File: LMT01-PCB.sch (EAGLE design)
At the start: 27 parts, among them IC1 PIC18F47K40, IC2 +12v, IC3 LM393D, IC4 MAX3467CPA, IC5 LM393D

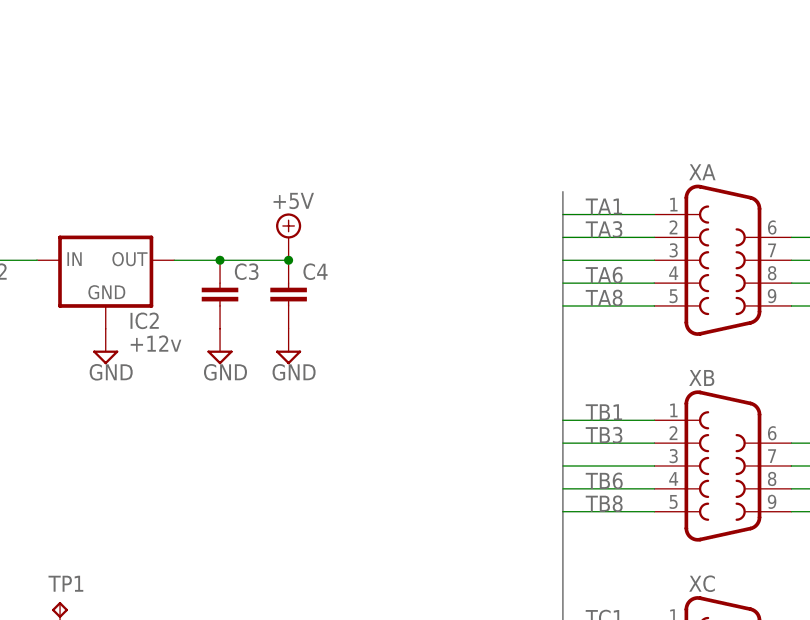
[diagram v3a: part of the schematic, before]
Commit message: Adding power LED
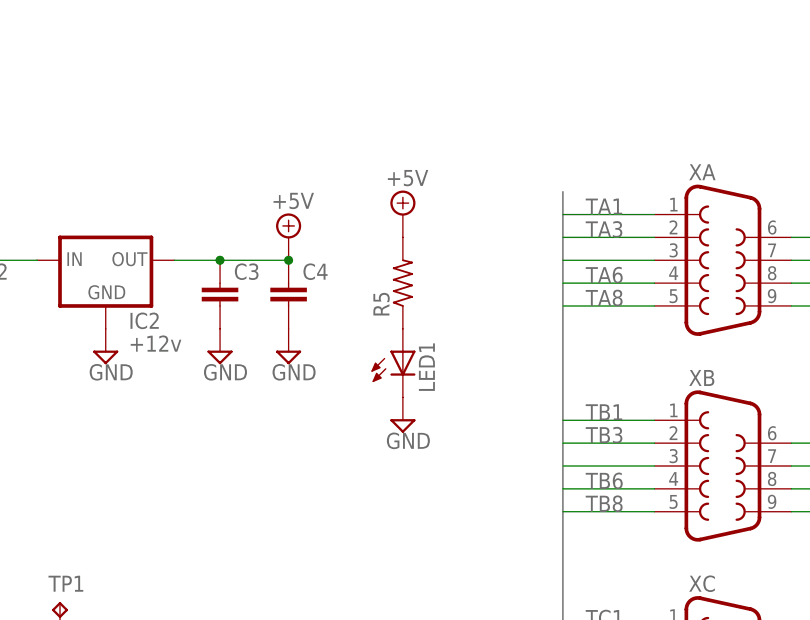
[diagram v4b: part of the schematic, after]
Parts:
- added LED1: (no value), led:LEDCHIPLED_1206
- added R5: (no value), resistor:R-US_R1206
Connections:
- new net N$5: LED1.A, R5.1
- net +5V: now also R5.2
- net GND: now also LED1.C
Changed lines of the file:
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@@
 <part name="JP4" library="SparkFun-Jumpers" deviceset="JUMPER-SMT_2_NO" device="_SILK"/>
 <part name="JP5" library="SparkFun-Jumpers" deviceset="JUMPER-SMT_2_NO" device="_SILK"/>
+<part name="LED1" library="led" deviceset="LED" device="CHIPLED_1206"/>
+<part name="R5" library="resistor" deviceset="R-US_" device="R1206"/>
+<part name="SUPPLY32" library="supply2" deviceset="GND" device=""/>
+<part name="SUPPLY33" library="supply2" deviceset="+5V" device=""/>
 </parts>
 <sheets>
@@
 <instance part="JP4" gate="G$1" x="111.76" y="-35.56"/>
 <instance part="JP5" gate="G$1" x="154.94" y="-35.56"/>
+<instance part="LED1" gate="G$1" x="-7.62" y="10.16"/>
+<instance part="R5" gate="G$1" x="-7.62" y="17.78" rot="R90"/>
+<instance part="SUPPLY32" gate="GND" x="-7.62" y="2.54"/>
+<instance part="SUPPLY33" gate="+5V" x="-7.62" y="25.4"/>
 </instances>
 <busses>
@@
 <pinref part="SUPPLY29" gate="+5V" pin="+5V"/>
 </segment>
+<segment>
+<pinref part="R5" gate="G$1" pin="2"/>
+<pinref part="SUPPLY33" gate="+5V" pin="+5V"/>
+</segment>
 </net>
 <net name="GND" class="0">
@@
 <pinref part="IC5" gate="P" pin="V-"/>
 <pinref part="SUPPLY31" gate="GND" pin="GND"/>
+</segment>
+<segment>
+<pinref part="LED1" gate="G$1" pin="C"/>
+<pinref part="SUPPLY32" gate="GND" pin="GND"/>
 </segment>
 </net>
@@
 </segment>
 </net>
+<net name="N$5" class="0">
+<segment>
+<pinref part="LED1" gate="G$1" pin="A"/>
+<pinref part="R5" gate="G$1" pin="1"/>
+</segment>
+</net>

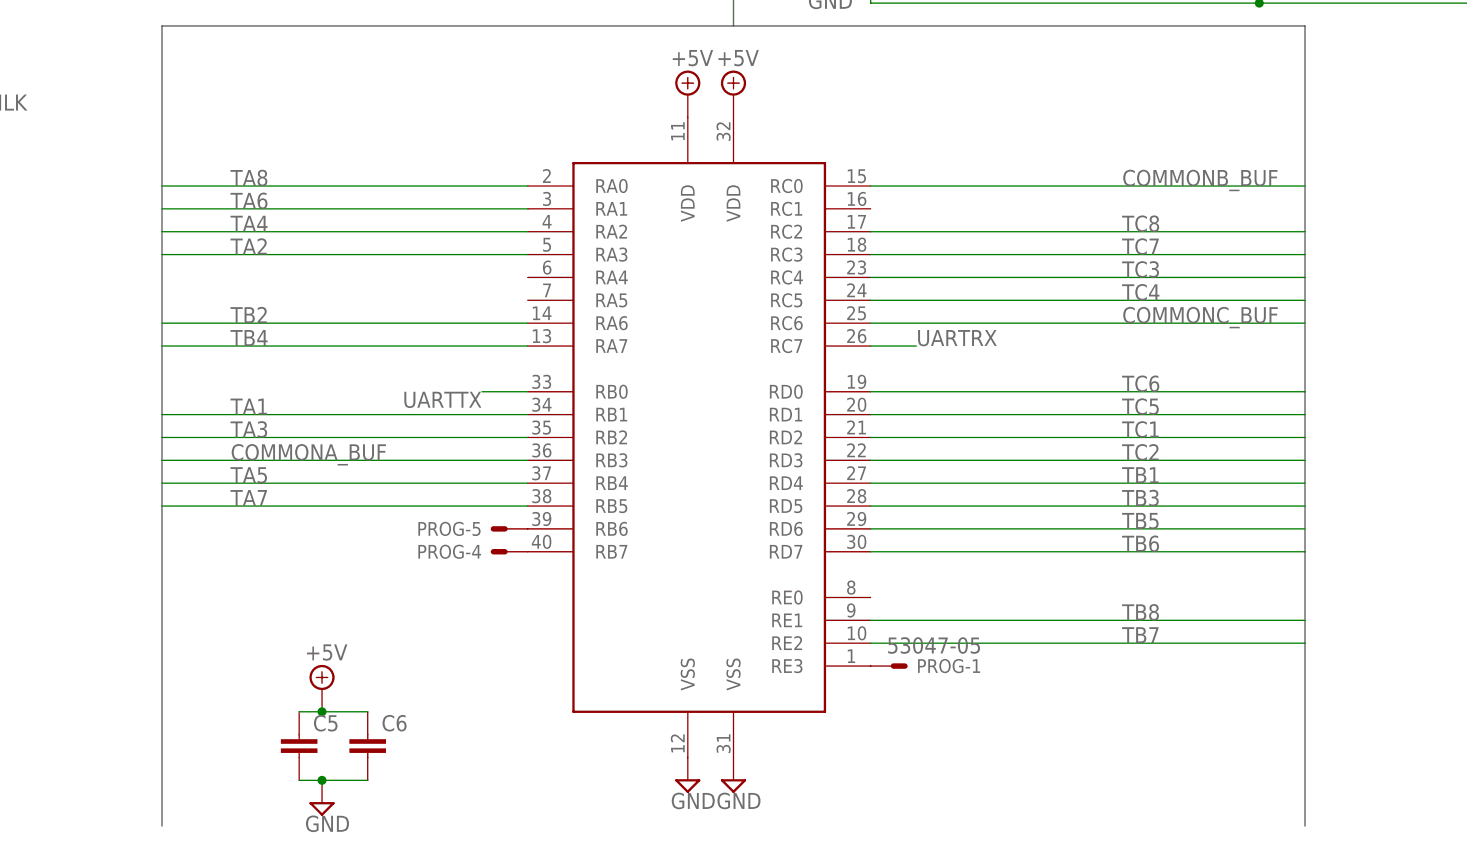
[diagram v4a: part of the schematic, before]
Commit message: Upgrading to PIC18F47Q84
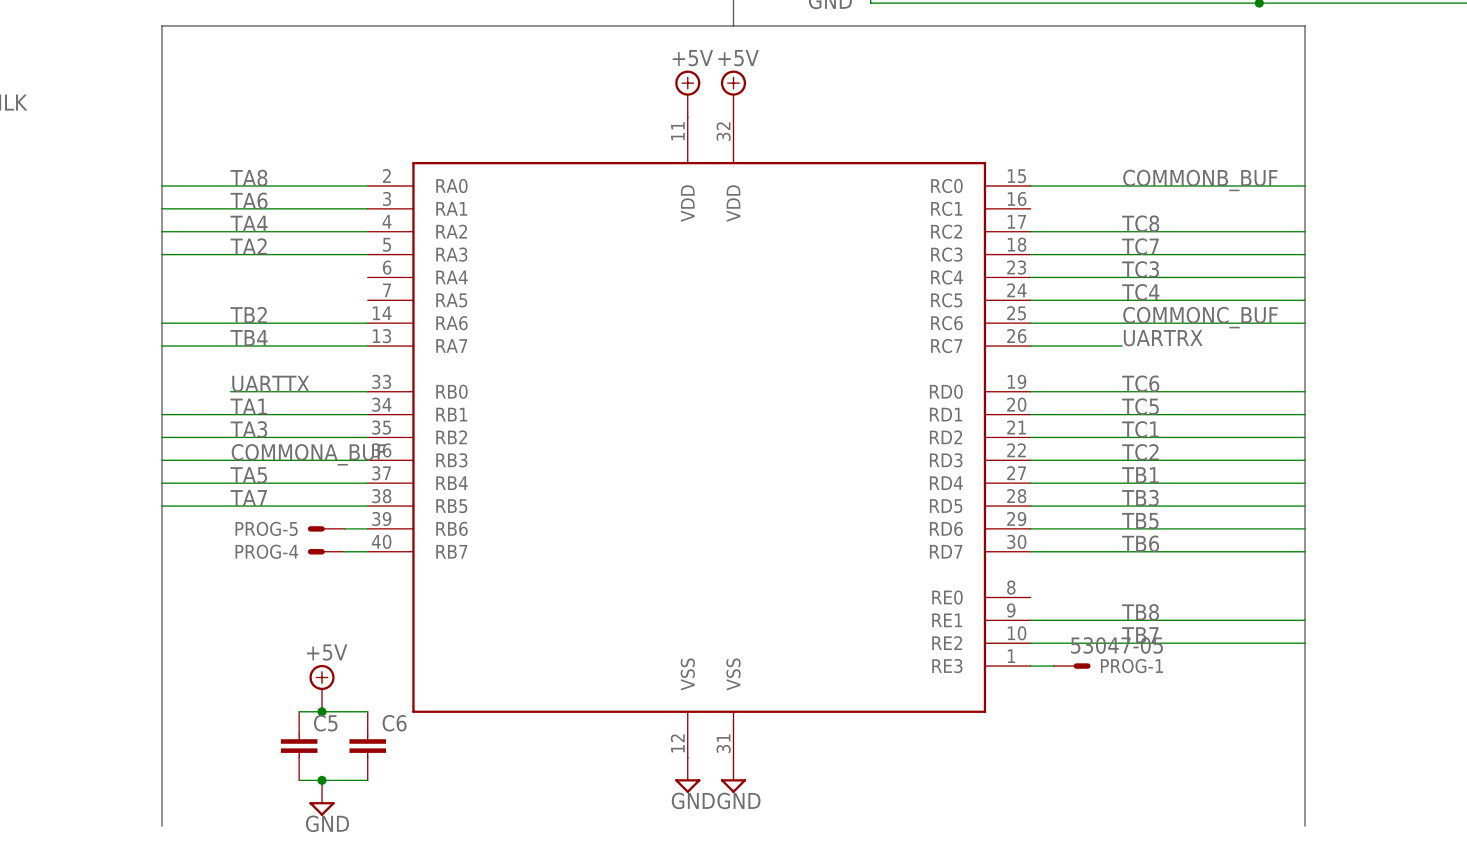
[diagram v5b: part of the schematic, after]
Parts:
- IC1: value PIC18F47K40 -> PIC18F47Q84; device microchip:PIC18F47K40 -> FRC696:PIC18F47Q84
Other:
- moved on the sheet: PROG-1, PROG-4, PROG-5

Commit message: Pin names
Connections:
- net N$1: now also IC1.RE3/!MCLR; no longer IC1.RE3
- net N$2: now also IC1.RB7/PGD; no longer IC1.RB7
- net N$3: now also IC1.RB6/PGC; no longer IC1.RB6
- net TB2: now also IC1.RA6/CLKOUT; no longer IC1.RA6
- net TB4: now also IC1.RA7/CLKIN; no longer IC1.RA7
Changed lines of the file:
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@@
 </segment>
 <segment>
-<pinref part="IC1" gate="G$1" pin="RA6"/>
+<pinref part="IC1" gate="G$1" pin="RA6/CLKOUT"/>
 <wire x1="5.08" y1="-106.68" x2="-17.78" y2="-106.68" width="0.1524" layer="91"/>
 <label x="-10.16" y="-106.68" size="1.778" layer="95"/>
@@
 </segment>
 <segment>
-<pinref part="IC1" gate="G$1" pin="RA7"/>
+<pinref part="IC1" gate="G$1" pin="RA7/CLKIN"/>
 <wire x1="5.08" y1="-109.22" x2="-17.78" y2="-109.22" width="0.1524" layer="91"/>
 <label x="-10.16" y="-109.22" size="1.778" layer="95"/>
@@
 <net name="N$1" class="0">
 <segment>
-<pinref part="IC1" gate="G$1" pin="RE3"/>
+<pinref part="IC1" gate="G$1" pin="RE3/!MCLR"/>
 <pinref part="PROG" gate="-1" pin="S"/>
 <wire x1="81.28" y1="-144.78" x2="78.74" y2="-144.78" width="0.1524" layer="91"/>
@@
 <net name="N$2" class="0">
 <segment>
-<pinref part="IC1" gate="G$1" pin="RB7"/>
+<pinref part="IC1" gate="G$1" pin="RB7/PGD"/>
 <pinref part="PROG" gate="-4" pin="S"/>
 <wire x1="2.54" y1="-132.08" x2="5.08" y2="-132.08" width="0.1524" layer="91"/>
@@
 <net name="N$3" class="0">
 <segment>
-<pinref part="IC1" gate="G$1" pin="RB6"/>
+<pinref part="IC1" gate="G$1" pin="RB6/PGC"/>
 <pinref part="PROG" gate="-5" pin="S"/>
 <wire x1="2.54" y1="-129.54" x2="5.08" y2="-129.54" width="0.1524" layer="91"/>

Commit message: Adding test points
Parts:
- added TP3, TP4, TP5: TPB1,27, testpad:TPB1,27
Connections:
- net N$21 renamed TX+
- net N$22 renamed TX-
- net N$23 renamed RX+
- net N$24 renamed RX-
- new net N$6: IC1.RA5, TP4.TP
- new net N$7: IC1.RE0, TP5.TP
- net N$4: now also TP3.TP
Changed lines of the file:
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@@
 <part name="SUPPLY32" library="supply2" deviceset="GND" device=""/>
 <part name="SUPPLY33" library="supply2" deviceset="+5V" device=""/>
+<part name="TP3" library="testpad" deviceset="TP" device="B1,27"/>
+<part name="TP4" library="testpad" deviceset="TP" device="B1,27"/>
+<part name="TP5" library="testpad" deviceset="TP" device="B1,27"/>
 </parts>
 <sheets>
@@
 <instance part="SUPPLY32" gate="GND" x="-7.62" y="2.54"/>
 <instance part="SUPPLY33" gate="+5V" x="-7.62" y="25.4"/>
+<instance part="TP3" gate="G$1" x="170.18" y="-68.58"/>
+<instance part="TP4" gate="G$1" x="2.54" y="-104.14" rot="R90"/>
+<instance part="TP5" gate="G$1" x="81.28" y="-137.16" rot="R270"/>
 </instances>
 <busses>
@@
 </segment>
 </net>
-<net name="N$21" class="0">
+<net name="TX+" class="0">
 <segment>
 <pinref part="IC4" gate="G$1" pin="Y"/>
@@
 </segment>
 </net>
-<net name="N$22" class="0">
+<net name="TX-" class="0">
 <segment>
 <pinref part="IC4" gate="G$1" pin="Z"/>
@@
 </segment>
 </net>
-<net name="N$23" class="0">
+<net name="RX+" class="0">
 <segment>
 <pinref part="IC4" gate="G$1" pin="A"/>
@@
 </segment>
 </net>
-<net name="N$24" class="0">
+<net name="RX-" class="0">
 <segment>
 <pinref part="IC4" gate="G$1" pin="B"/>
@@
 <pinref part="XA" gate="G$1" pin="3"/>
 <wire x1="20.32" y1="20.32" x2="10.16" y2="20.32" width="0.1524" layer="91"/>
+<label x="12.7" y="20.32" size="1.778" layer="95"/>
 </segment>
 <segment>
@@
 <pinref part="IC5" gate="A" pin="-IN"/>
 <wire x1="104.14" y1="-71.12" x2="144.78" y2="-71.12" width="0.1524" layer="91"/>
-<wire x1="144.78" y1="-71.12" x2="185.42" y2="-71.12" width="0.1524" layer="91"/>
+<wire x1="144.78" y1="-71.12" x2="170.18" y2="-71.12" width="0.1524" layer="91"/>
+<wire x1="170.18" y1="-71.12" x2="185.42" y2="-71.12" width="0.1524" layer="91"/>
 <wire x1="104.14" y1="-53.34" x2="104.14" y2="-71.12" width="0.1524" layer="91"/>
 <junction x="104.14" y="-71.12"/>
@@
 <wire x1="144.78" y1="-53.34" x2="144.78" y2="-71.12" width="0.1524" layer="91"/>
 <junction x="144.78" y="-71.12"/>
+<pinref part="TP3" gate="G$1" pin="TP"/>
+<junction x="170.18" y="-71.12"/>
 </segment>
 </net>
@@
 </segment>
 </net>
+<net name="N$6" class="0">
+<segment>
+<pinref part="IC1" gate="G$1" pin="RA5"/>
+<pinref part="TP4" gate="G$1" pin="TP"/>
+</segment>
+</net>
+<net name="N$7" class="0">
+<segment>
+<pinref part="IC1" gate="G$1" pin="RE0"/>
+<pinref part="TP5" gate="G$1" pin="TP"/>
+</segment>
+</net>

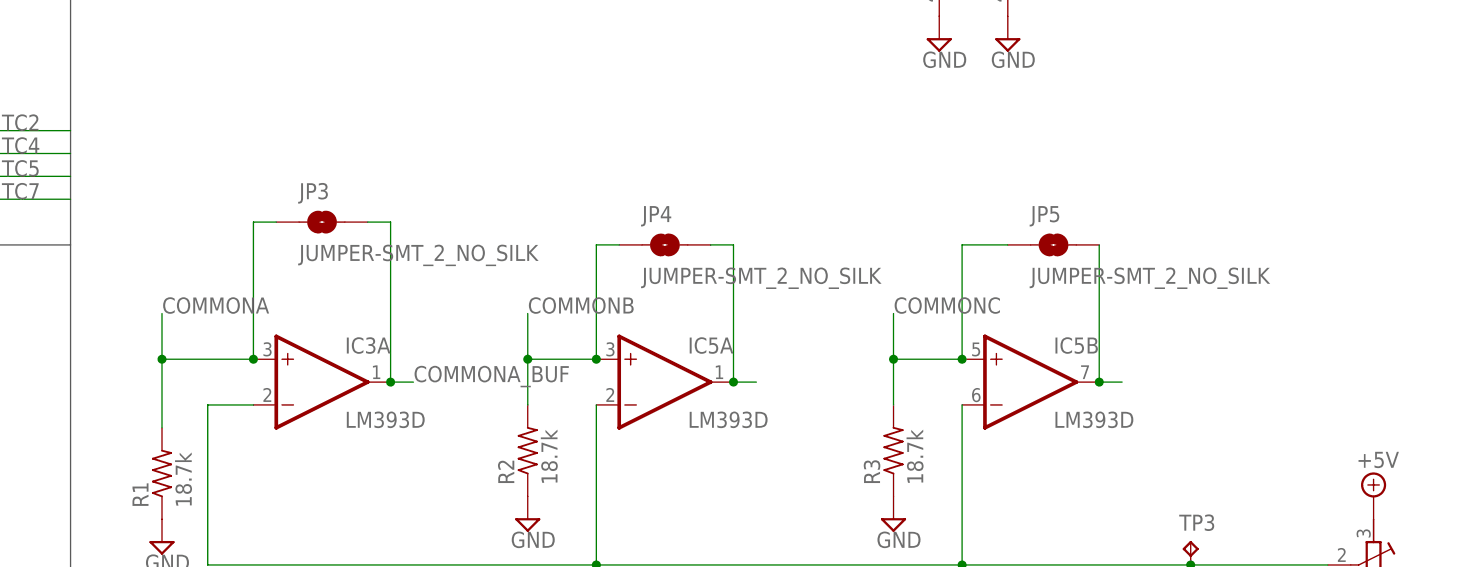
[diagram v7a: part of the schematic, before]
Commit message: Adding more test points and deleting jumpers
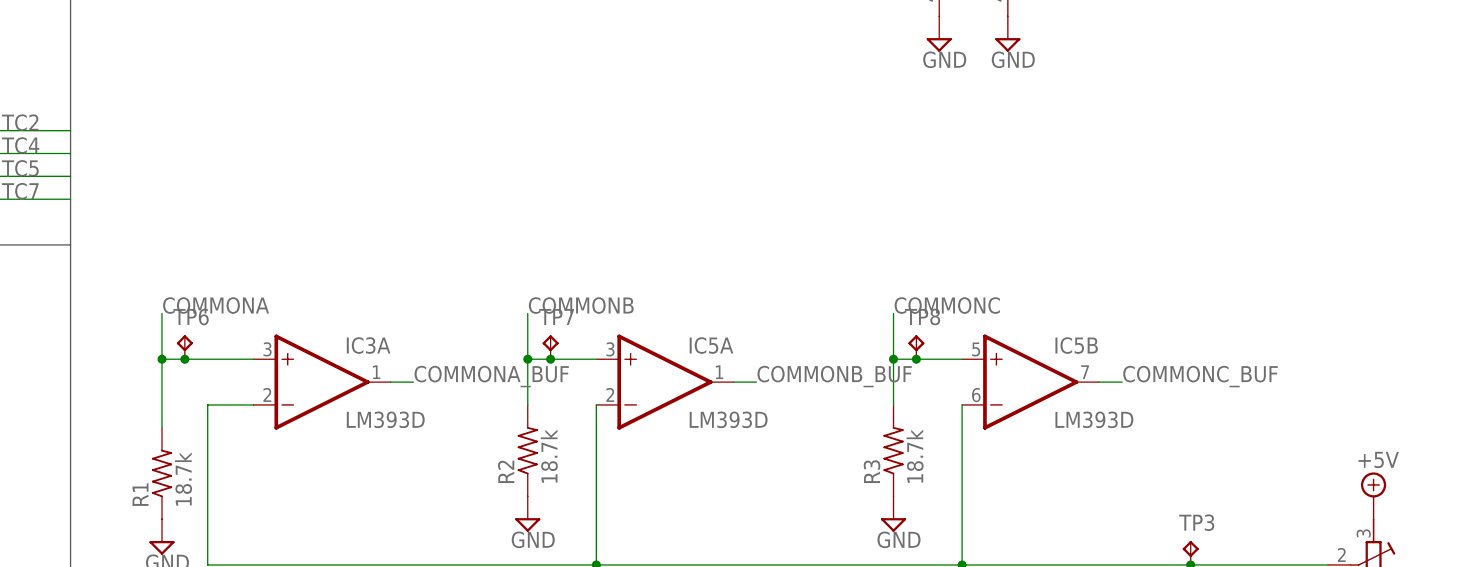
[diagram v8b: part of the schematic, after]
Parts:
- removed JP3, JP4, JP5: JUMPER-SMT_2_NO_SILK, SparkFun-Jumpers:JUMPER-SMT_2_NO_SILK
- added TP6, TP7, TP8: TPB1,27, testpad:TPB1,27
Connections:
- net COMMONA: now also TP6.TP; no longer JP3.1
- net COMMONA_BUF: no longer JP3.2
- net COMMONB: now also TP7.TP; no longer JP4.1
- net COMMONB_BUF: no longer JP4.2
- net COMMONC: now also TP8.TP; no longer JP5.1
- net COMMONC_BUF: no longer JP5.2
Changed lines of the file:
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@@
 <part name="SUPPLY30" library="supply2" deviceset="GND" device=""/>
 <part name="SUPPLY31" library="supply2" deviceset="GND" device=""/>
-<part name="JP3" library="SparkFun-Jumpers" deviceset="JUMPER-SMT_2_NO" device="_SILK"/>
-<part name="JP4" library="SparkFun-Jumpers" deviceset="JUMPER-SMT_2_NO" device="_SILK"/>
-<part name="JP5" library="SparkFun-Jumpers" deviceset="JUMPER-SMT_2_NO" device="_SILK"/>
 <part name="LED1" library="led" deviceset="LED" device="CHIPLED_1206"/>
 <part name="R5" library="resistor" deviceset="R-US_" device="R1206"/>
@@
 <part name="TP4" library="testpad" deviceset="TP" device="B1,27"/>
 <part name="TP5" library="testpad" deviceset="TP" device="B1,27"/>
+<part name="TP6" library="testpad" deviceset="TP" device="B1,27"/>
+<part name="TP7" library="testpad" deviceset="TP" device="B1,27"/>
+<part name="TP8" library="testpad" deviceset="TP" device="B1,27"/>
 </parts>
 <sheets>
@@
 <instance part="SUPPLY30" gate="GND" x="142.24" y="-12.7"/>
 <instance part="SUPPLY31" gate="GND" x="149.86" y="-12.7"/>
-<instance part="JP3" gate="G$1" x="73.66" y="-33.02"/>
-<instance part="JP4" gate="G$1" x="111.76" y="-35.56"/>
-<instance part="JP5" gate="G$1" x="154.94" y="-35.56"/>
 <instance part="LED1" gate="G$1" x="-7.62" y="10.16"/>
 <instance part="R5" gate="G$1" x="-7.62" y="17.78" rot="R90"/>
@@
 <instance part="TP4" gate="G$1" x="2.54" y="-104.14" rot="R90"/>
 <instance part="TP5" gate="G$1" x="81.28" y="-137.16" rot="R270"/>
+<instance part="TP6" gate="G$1" x="58.42" y="-45.72"/>
+<instance part="TP7" gate="G$1" x="99.06" y="-45.72"/>
+<instance part="TP8" gate="G$1" x="139.7" y="-45.72"/>
 </instances>
 <busses>
@@
 <wire x1="55.88" y1="-48.26" x2="55.88" y2="-43.18" width="0.1524" layer="91"/>
 <junction x="55.88" y="-48.26"/>
-<pinref part="JP3" gate="G$1" pin="1"/>
-<wire x1="66.04" y1="-48.26" x2="55.88" y2="-48.26" width="0.1524" layer="91"/>
-<wire x1="68.58" y1="-33.02" x2="66.04" y2="-33.02" width="0.1524" layer="91"/>
-<wire x1="66.04" y1="-33.02" x2="66.04" y2="-48.26" width="0.1524" layer="91"/>
-<junction x="66.04" y="-48.26"/>
+<wire x1="66.04" y1="-48.26" x2="58.42" y2="-48.26" width="0.1524" layer="91"/>
+<pinref part="TP6" gate="G$1" pin="TP"/>
+<wire x1="58.42" y1="-48.26" x2="55.88" y2="-48.26" width="0.1524" layer="91"/>
+<junction x="58.42" y="-48.26"/>
 </segment>
 </net>
@@
 <pinref part="IC5" gate="A" pin="+IN"/>
 <wire x1="96.52" y1="-48.26" x2="96.52" y2="-43.18" width="0.1524" layer="91"/>
-<wire x1="104.14" y1="-48.26" x2="96.52" y2="-48.26" width="0.1524" layer="91"/>
+<wire x1="104.14" y1="-48.26" x2="99.06" y2="-48.26" width="0.1524" layer="91"/>
 <junction x="96.52" y="-48.26"/>
-<pinref part="JP4" gate="G$1" pin="1"/>
-<wire x1="106.68" y1="-35.56" x2="104.14" y2="-35.56" width="0.1524" layer="91"/>
-<wire x1="104.14" y1="-35.56" x2="104.14" y2="-48.26" width="0.1524" layer="91"/>
-<junction x="104.14" y="-48.26"/>
+<pinref part="TP7" gate="G$1" pin="TP"/>
+<wire x1="99.06" y1="-48.26" x2="96.52" y2="-48.26" width="0.1524" layer="91"/>
+<junction x="99.06" y="-48.26"/>
 </segment>
 </net>
@@
 <pinref part="IC5" gate="B" pin="+IN"/>
 <wire x1="137.16" y1="-48.26" x2="137.16" y2="-43.18" width="0.1524" layer="91"/>
-<wire x1="144.78" y1="-48.26" x2="137.16" y2="-48.26" width="0.1524" layer="91"/>
+<wire x1="144.78" y1="-48.26" x2="139.7" y2="-48.26" width="0.1524" layer="91"/>
 <junction x="137.16" y="-48.26"/>
-<pinref part="JP5" gate="G$1" pin="1"/>
-<wire x1="149.86" y1="-35.56" x2="144.78" y2="-35.56" width="0.1524" layer="91"/>
-<wire x1="144.78" y1="-35.56" x2="144.78" y2="-48.26" width="0.1524" layer="91"/>
-<junction x="144.78" y="-48.26"/>
+<pinref part="TP8" gate="G$1" pin="TP"/>
+<wire x1="139.7" y1="-48.26" x2="137.16" y2="-48.26" width="0.1524" layer="91"/>
+<junction x="139.7" y="-48.26"/>
 </segment>
 </net>
@@
 <wire x1="81.28" y1="-50.8" x2="83.82" y2="-50.8" width="0.1524" layer="91"/>
 <label x="83.82" y="-50.8" size="1.778" layer="95"/>
-<pinref part="JP3" gate="G$1" pin="2"/>
-<wire x1="78.74" y1="-33.02" x2="81.28" y2="-33.02" width="0.1524" layer="91"/>
-<wire x1="81.28" y1="-33.02" x2="81.28" y2="-50.8" width="0.1524" layer="91"/>
-<junction x="81.28" y="-50.8"/>
 </segment>
 <segment>
@@
 <pinref part="IC5" gate="A" pin="OUT"/>
 <wire x1="119.38" y1="-50.8" x2="121.92" y2="-50.8" width="0.1524" layer="91"/>
-<pinref part="JP4" gate="G$1" pin="2"/>
-<wire x1="116.84" y1="-35.56" x2="119.38" y2="-35.56" width="0.1524" layer="91"/>
-<wire x1="119.38" y1="-35.56" x2="119.38" y2="-50.8" width="0.1524" layer="91"/>
-<junction x="119.38" y="-50.8"/>
+<label x="121.92" y="-50.8" size="1.778" layer="95"/>
 </segment>
 </net>
@@
 <pinref part="IC5" gate="B" pin="OUT"/>
 <wire x1="160.02" y1="-50.8" x2="162.56" y2="-50.8" width="0.1524" layer="91"/>
-<pinref part="JP5" gate="G$1" pin="2"/>
-<wire x1="160.02" y1="-35.56" x2="160.02" y2="-50.8" width="0.1524" layer="91"/>
-<junction x="160.02" y="-50.8"/>
-</segment>
-</net>
+<label x="162.56" y="-50.8" size="1.778" layer="95"/>
+</segment>
+</net>
